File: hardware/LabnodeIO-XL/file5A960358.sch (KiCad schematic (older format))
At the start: 2 parts, among them U7 PCF8574

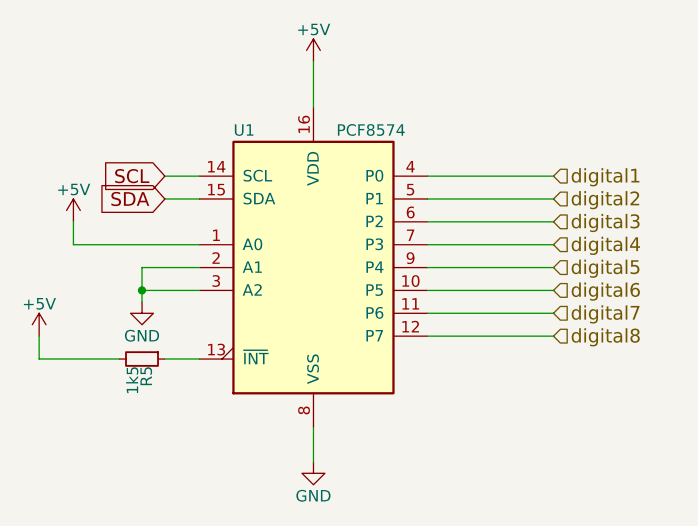
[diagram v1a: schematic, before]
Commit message: eingangswiderstände hinzugefuegt und geroutet
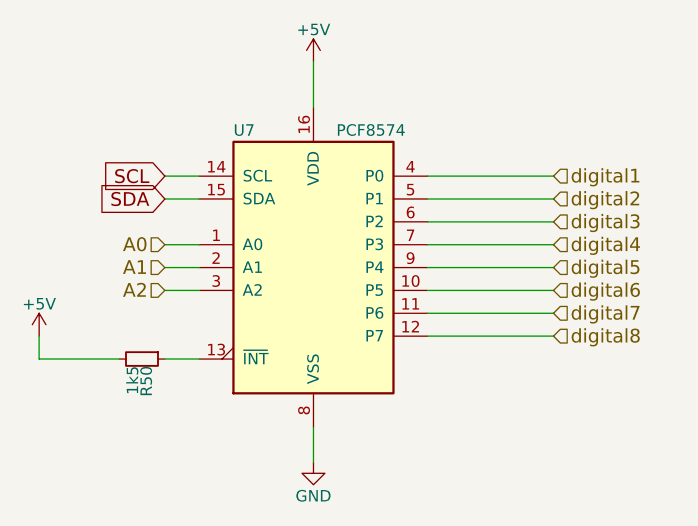
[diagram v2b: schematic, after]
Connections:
- net +5V: no longer U7.1 (A0)
- net GND: no longer U7.2 (A1), U7.3 (A2)
- new net A0: U7.1 (A0)
- new net A1: U7.2 (A1)
- new net A2: U7.3 (A2)
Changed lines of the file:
@@
 $Descr A4 11693 8268
 encoding utf-8
-Sheet 7 7
+Sheet 4 7
 Title ""
 Date ""
@@
 AR Path="/5A960B2A/5A96057F" Ref="U7"  Part="1"
 AR Path="/5A960359/5A96057F" Ref="U1"  Part="1"
-F 0 "U1" H 4050 3300 50  0000 L CNN
+F 0 "U7" H 4050 3300 50  0000 L CNN
 F 1 "PCF8574" H 4500 3300 50  0000 L CNN
 F 2 "Housings_SOIC:SOIC-16W_7.5x12.8mm_Pitch1.27mm" H 4400 2700 50  0001 C CNN
@@
 $EndComp
 $Comp
-L +5V #PWR052
+L +5V #PWR89
 U 1 1 5A960586
 P 4400 1800
-AR Path="/5A960B2A/5A960586" Ref="#PWR052"  Part="1"
-AR Path="/5A960359/5A960586" Ref="#PWR047"  Part="1"
-F 0 "#PWR047" H 4400 1650 50  0001 C CNN
+AR Path="/5A960B2A/5A960586" Ref="#PWR89"  Part="1"
+AR Path="/5A960359/5A960586" Ref="#PWR54"  Part="1"
+F 0 "#PWR89" H 4400 1650 50  0001 C CNN
 F 1 "+5V" H 4400 1940 50  0000 C CNN
 F 2 "" H 4400 1800 50  0001 C CNN
@@
 $EndComp
 $Comp
-L GND #PWR053
+L GND #PWR90
 U 1 1 5A96058C
 P 4400 3550
-AR Path="/5A960B2A/5A96058C" Ref="#PWR053"  Part="1"
-AR Path="/5A960359/5A96058C" Ref="#PWR048"  Part="1"
-F 0 "#PWR048" H 4400 3300 50  0001 C CNN
+AR Path="/5A960B2A/5A96058C" Ref="#PWR90"  Part="1"
+AR Path="/5A960359/5A96058C" Ref="#PWR55"  Part="1"
+F 0 "#PWR90" H 4400 3300 50  0001 C CNN
 F 1 "GND" H 4400 3400 50  0000 C CNN
 F 2 "" H 4400 3550 50  0001 C CNN
@@
 $EndComp
 $Comp
-L GND #PWR049
-U 1 1 5A960592
-P 3650 2850
-AR Path="/5A960359/5A960592" Ref="#PWR049"  Part="1"
-AR Path="/5A960B2A/5A960592" Ref="#PWR054"  Part="1"
-F 0 "#PWR049" H 3650 2600 50  0001 C CNN
-F 1 "GND" H 3650 2700 50  0000 C CNN
-F 2 "" H 3650 2850 50  0001 C CNN
-F 3 "" H 3650 2850 50  0001 C CNN
-	1    3650 2850
-	1    0    0    -1
-$EndComp
-$Comp
-L +5V #PWR050
+L +5V #PWR53
 U 1 1 5A960598
 P 3200 3000
-AR Path="/5A960359/5A960598" Ref="#PWR050"  Part="1"
-AR Path="/5A960B2A/5A960598" Ref="#PWR055"  Part="1"
-F 0 "#PWR050" H 3200 2850 50  0001 C CNN
+AR Path="/5A960359/5A960598" Ref="#PWR53"  Part="1"
+AR Path="/5A960B2A/5A960598" Ref="#PWR88"  Part="1"
+F 0 "#PWR88" H 3200 2850 50  0001 C CNN
 F 1 "+5V" H 3200 3140 50  0000 C CNN
 F 2 "" H 3200 3000 50  0001 C CNN
@@
 AR Path="/5A960B2A/5A9605AD" Ref="R50"  Part="1"
 AR Path="/5A960359/5A9605AD" Ref="R5"  Part="1"
-F 0 "R5" H 3680 3120 50  0000 L CNN
+F 0 "R50" H 3680 3120 50  0000 L CNN
 F 1 "1k5" H 3680 3060 50  0000 L CNN
 F 2 "Resistors_SMD:R_0603" H 3650 3100 50  0001 C CNN
@@
 Wire Wire Line
 	4400 3550 4400 3400
-Wire Wire Line
-	3350 2600 3900 2600
-Wire Wire Line
-	3900 2700 3650 2700
-Wire Wire Line
-	3900 2800 3650 2800
-Connection ~ 3650 2800
 Wire Wire Line
 	5450 2300 4900 2300
@@
 Text HLabel 5450 3000 2    60   Input ~ 0
 digital8
-$Comp
-L +5V #PWR056
-U 1 1 5A960CD3
-P 3350 2500
-AR Path="/5A960B2A/5A960CD3" Ref="#PWR056"  Part="1"
-AR Path="/5A960359/5A960CD3" Ref="#PWR051"  Part="1"
-F 0 "#PWR051" H 3350 2350 50  0001 C CNN
-F 1 "+5V" H 3350 2640 50  0000 C CNN
-F 2 "" H 3350 2500 50  0001 C CNN
-F 3 "" H 3350 2500 50  0001 C CNN
-	1    3350 2500
-	1    0    0    -1
-$EndComp
+Text HLabel 3750 2600 0    60   Input ~ 0
+A0
+Text HLabel 3750 2700 0    60   Input ~ 0
+A1
+Text HLabel 3750 2800 0    60   Input ~ 0
+A2
 Wire Wire Line
-	3350 2500 3350 2600
+	3750 2600 3900 2600
 Wire Wire Line
-	3650 2700 3650 2850
+	3900 2700 3750 2700
+Wire Wire Line
+	3750 2800 3900 2800
 $EndSCHEMATC
